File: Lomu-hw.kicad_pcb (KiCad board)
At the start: 2 copper layers, 30 x 26.8 mm, 1 part

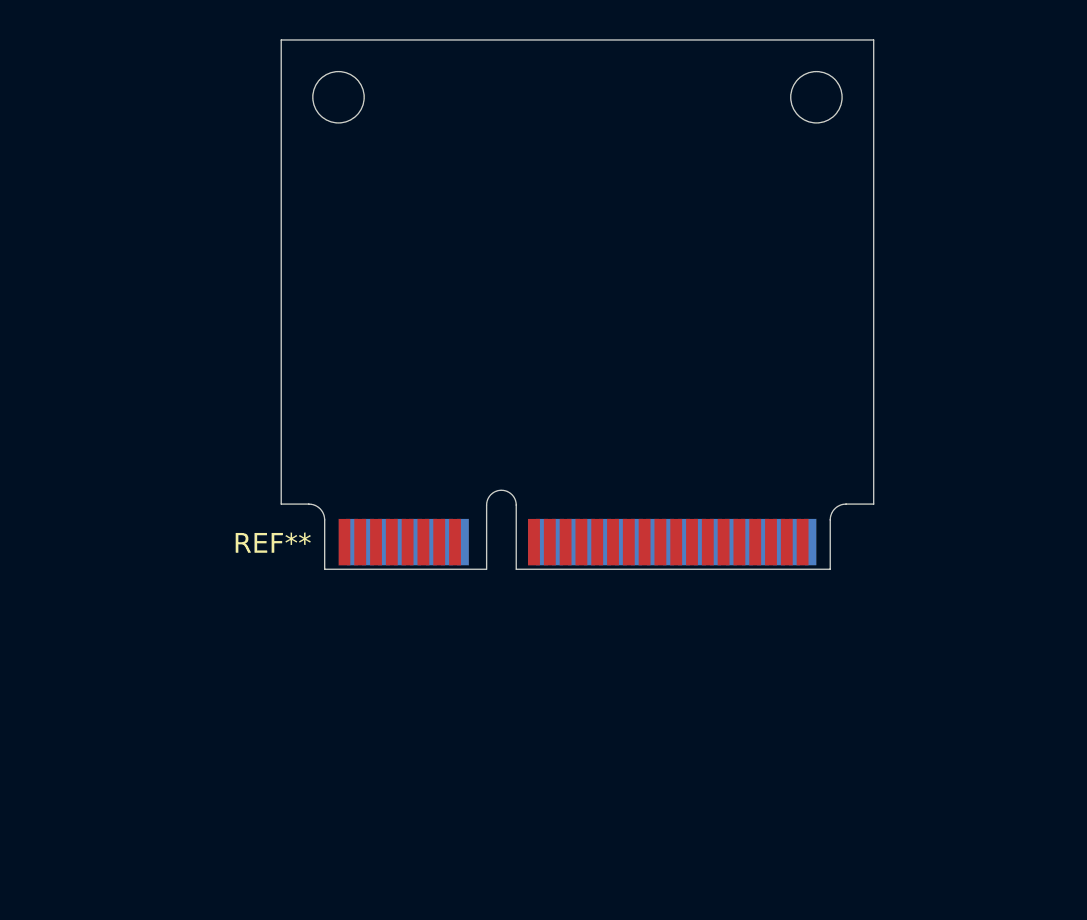
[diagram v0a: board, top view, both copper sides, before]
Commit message: Updates project from mPCIe F1 template
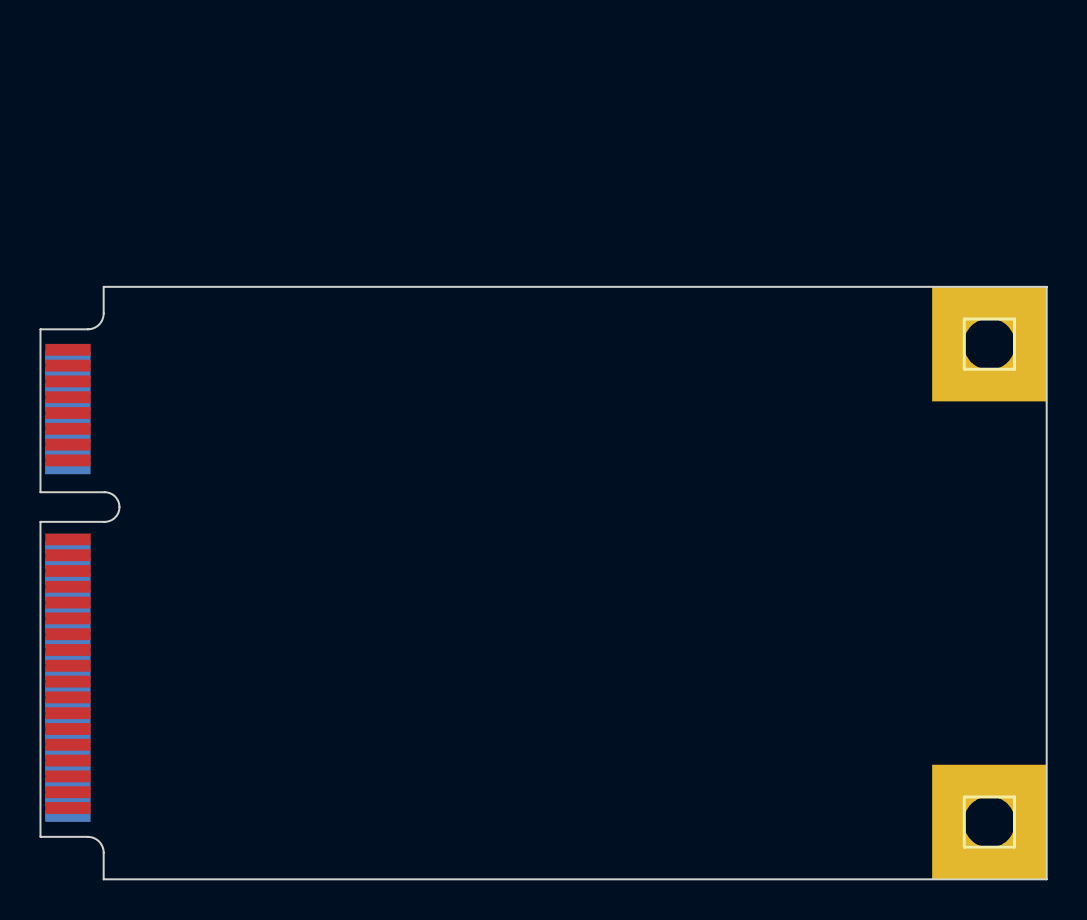
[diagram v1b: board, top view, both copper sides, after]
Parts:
- removed REF**: mini-PCIe_H1_Half, mpcie:mini-PCIe_H1_Half
- added J1: PCIE-MINI, mini-PCIe:miniPCIeConn, F.Cu at (116.5, 61.6)
- added MOUNTING_HOLE1: CONN_1, PIN_ARRAY_1, F.Cu at (163.1, 53.4)
- added MOUNTING_HOLE2: CONN_1, PIN_ARRAY_1, F.Cu at (163.1, 77.6)
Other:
- board size 30 x 26.8 mm -> 50.9 x 30 mm

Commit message: Adds first draft of layout
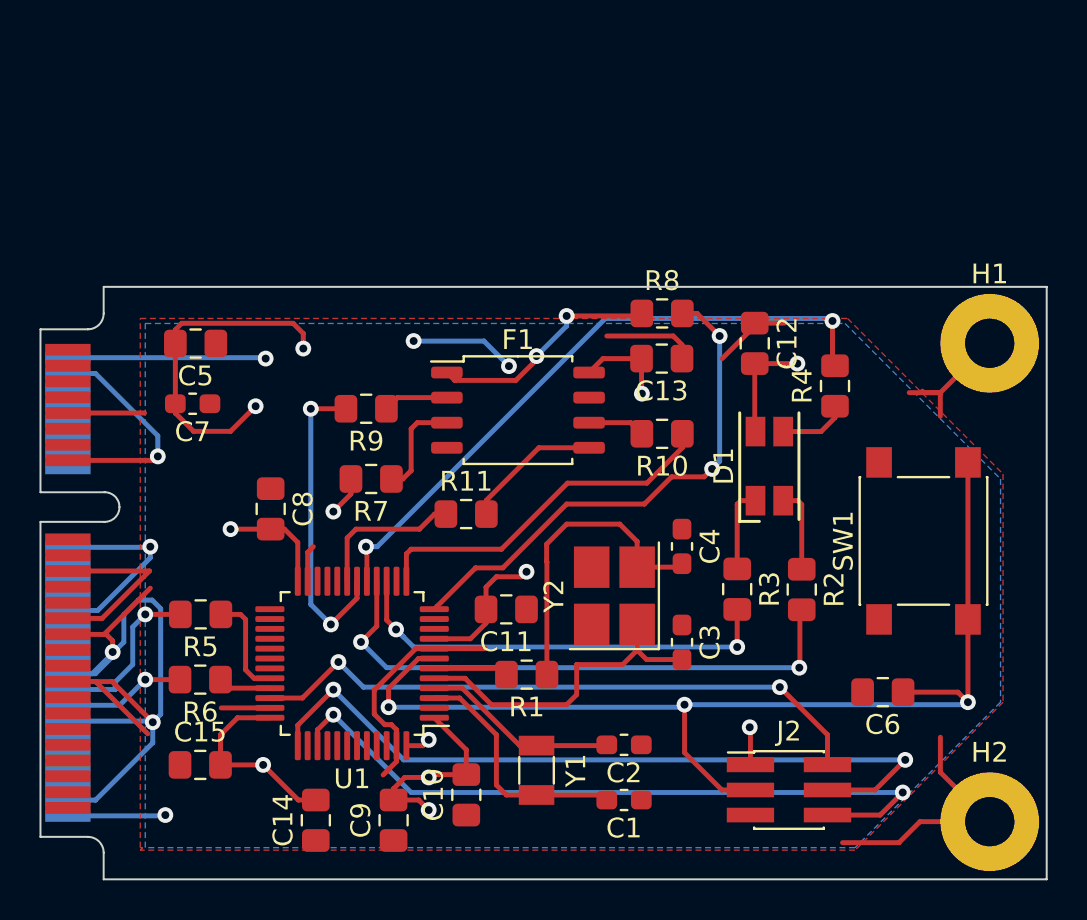
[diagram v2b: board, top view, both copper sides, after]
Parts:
- removed MOUNTING_HOLE1, MOUNTING_HOLE2: CONN_1, PIN_ARRAY_1
- added C1: 10pF, Capacitor_SMD:C_0603_1608Metric_Pad1.05x0.95mm_HandSolder, F.Cu at (144.6, 76.5)
- added C10: 100nF, Capacitor_SMD:C_0805_2012Metric_Pad1.15x1.40mm_HandSolder, F.Cu at (136.7, 76.2)
- added C11: 100nF, Capacitor_SMD:C_0805_2012Metric_Pad1.15x1.40mm_HandSolder, F.Cu at (138.7, 66.8)
- added C12: 100nF, Capacitor_SMD:C_0805_2012Metric_Pad1.15x1.40mm_HandSolder, F.Cu at (151.3, 53.3)
- added C13: 100nF, Capacitor_SMD:C_0805_2012Metric_Pad1.15x1.40mm_HandSolder, F.Cu at (146.5, 54.1)
- added C14: 4.7uF, Capacitor_SMD:C_0805_2012Metric_Pad1.15x1.40mm_HandSolder, F.Cu at (129.0, 77.5)
- added C15: 100nF, Capacitor_SMD:C_0805_2012Metric_Pad1.15x1.40mm_HandSolder, F.Cu at (123.2, 74.7)
- added C2: 10pF, Capacitor_SMD:C_0603_1608Metric_Pad1.05x0.95mm_HandSolder, F.Cu at (144.6, 73.7)
- added C3: 20pF, Capacitor_SMD:C_0603_1608Metric_Pad1.05x0.95mm_HandSolder, F.Cu at (147.6, 68.5)
- added C4: 20pF, Capacitor_SMD:C_0603_1608Metric_Pad1.05x0.95mm_HandSolder, F.Cu at (147.6, 63.6)
- added C5: 100nF, Capacitor_SMD:C_0805_2012Metric_Pad1.15x1.40mm_HandSolder, F.Cu at (122.9, 53.3)
- added C6: 100nF, Capacitor_SMD:C_0805_2012Metric_Pad1.15x1.40mm_HandSolder, F.Cu at (157.7, 71.0)
- added C7: 47pF, Capacitor_SMD:C_0603_1608Metric_Pad1.05x0.95mm_HandSolder, F.Cu at (122.8, 56.4)
- added C8: 100nF, Capacitor_SMD:C_0805_2012Metric_Pad1.15x1.40mm_HandSolder, F.Cu at (126.7, 61.7)
- added C9: 100nF, Capacitor_SMD:C_0805_2012Metric_Pad1.15x1.40mm_HandSolder, F.Cu at (133.0, 77.5)
- added D1: LED_RGBA, LED_SMD:LED_RGB_1210, F.Cu at (152.0, 59.5)
- added F1: MX25V1606FM2I03, Package_SO:SOP-8_5.28x5.23mm_P1.27mm, F.Cu at (139.3, 56.7)
- added H1: MountingHole_Pad, MountingHole:MountingHole_2.5mm_Pad, F.Cu at (163.2, 53.3)
- added H2: MountingHole_Pad, MountingHole:MountingHole_2.5mm_Pad, F.Cu at (163.2, 77.6)
- added J2: ARM_SWD_6, Connector_PinHeader_1.27mm:PinHeader_2x03_P1.27mm_Vertical_SMD, F.Cu at (153.0, 75.9)
- added R1: 390, Resistor_SMD:R_0805_2012Metric_Pad1.15x1.40mm_HandSolder, F.Cu at (139.7, 70.1)
- added R10: 33, Resistor_SMD:R_0805_2012Metric_Pad1.15x1.40mm_HandSolder, F.Cu at (146.6, 57.9)
- added R11: 33, Resistor_SMD:R_0805_2012Metric_Pad1.15x1.40mm_HandSolder, F.Cu at (136.6, 62.0)
- added R2: 1, Resistor_SMD:R_0805_2012Metric_Pad1.15x1.40mm_HandSolder, F.Cu at (153.6, 65.8)
- added R3: 68, Resistor_SMD:R_0805_2012Metric_Pad1.15x1.40mm_HandSolder, F.Cu at (150.4, 65.8)
- added R4: 1, Resistor_SMD:R_0805_2012Metric_Pad1.15x1.40mm_HandSolder, F.Cu at (155.3, 55.5)
- added R5: 22, Resistor_SMD:R_0805_2012Metric_Pad1.15x1.40mm_HandSolder, F.Cu at (123.2, 67.1)
- added R6: 22, Resistor_SMD:R_0805_2012Metric_Pad1.15x1.40mm_HandSolder, F.Cu at (123.2, 70.4)
- added R7: 10k, Resistor_SMD:R_0805_2012Metric_Pad1.15x1.40mm_HandSolder, F.Cu at (131.8, 60.2)
- added R8: 33, Resistor_SMD:R_0805_2012Metric_Pad1.15x1.40mm_HandSolder, F.Cu at (146.6, 51.8)
- added R9: 33, Resistor_SMD:R_0805_2012Metric_Pad1.15x1.40mm_HandSolder, F.Cu at (131.6, 56.6)
- added SW1: SW_Push_Dual, Button_Switch_SMD:SW_Push_1P1T_NO_6x6mm_H9.5mm, F.Cu at (159.8, 63.3)
- added U1: STM32L562CET6, Package_QFP:LQFP-48_7x7mm_P0.5mm, F.Cu at (130.9, 69.5)
- added Y1: 32 kHz, Crystal:Crystal_SMD_3215-2Pin_3.2x1.5mm, F.Cu at (140.2, 75.0)
- added Y2: 16 MHz, Crystal:Crystal_SMD_3225-4Pin_3.2x2.5mm_HandSoldering, F.Cu at (144.2, 66.1)
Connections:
- J1 pad 15: Net-(J1-Pad15) -> GND
- J1 pad 18: Net-(J1-Pad18) -> GND
- J1 pad 2: Net-(J1-Pad2) -> VCC
- J1 pad 21: Net-(J1-Pad21) -> GND
- J1 pad 26: Net-(J1-Pad26) -> GND
- J1 pad 27: Net-(J1-Pad27) -> GND
- J1 pad 29: Net-(J1-Pad29) -> GND
- J1 pad 34: Net-(J1-Pad34) -> GND
- J1 pad 35: Net-(J1-Pad35) -> GND
- J1 pad 4: Net-(J1-Pad4) -> GND
- J1 pad 40: Net-(J1-Pad40) -> GND
- J1 pad 50: Net-(J1-Pad50) -> GND
- J1 pad 52: Net-(J1-Pad52) -> VCC
- J1 pad 9: Net-(J1-Pad9) -> GND
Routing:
- net GND: track 0.00 -> 123.1 mm, vias 0 -> 4
- net VCC: track 0.00 -> 80.1 mm, vias 0 -> 14
- net /NRST: track 0.00 -> 55.5 mm, vias 0 -> 3
- net /TCK_SWCLK: track 0.00 -> 38.6 mm, vias 0 -> 2
- net /TDO_SWO: track 0.00 -> 36.7 mm, vias 0 -> 2
- net /LED3: track 0.00 -> 32.6 mm, vias 0 -> 2
- net /TMS_SWDIO: track 0.00 -> 32.0 mm, vias 0 -> 2
- net /LED2: track 0.00 -> 29.3 mm, vias 0 -> 2
- net /OCTOSPI1_NCS: track 0.00 -> 26.3 mm, vias 0 -> 2
- net /LED1: track 0.00 -> 22.9 mm, vias 0 -> 2
- net /OCTOSPI1_CLK: track 0.00 -> 18.3 mm
- net /OSC_IN: track 0.00 -> 16.6 mm
- net /OCTOSPI1_IO1: track 0.00 -> 15.9 mm, vias 0 -> 2
- net Net-(C4-Pad2): track 0.00 -> 15.6 mm
- net /OSC32_IN: track 0.00 -> 12.4 mm
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- added copper zone on F.Cu, net GND
- added copper zone on B.Cu, net VCC
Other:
- rule trace_min: 0.2 -> 0.25
- rule via_min_size: 0.4 -> 0.5

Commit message: Adds missing boot select trace
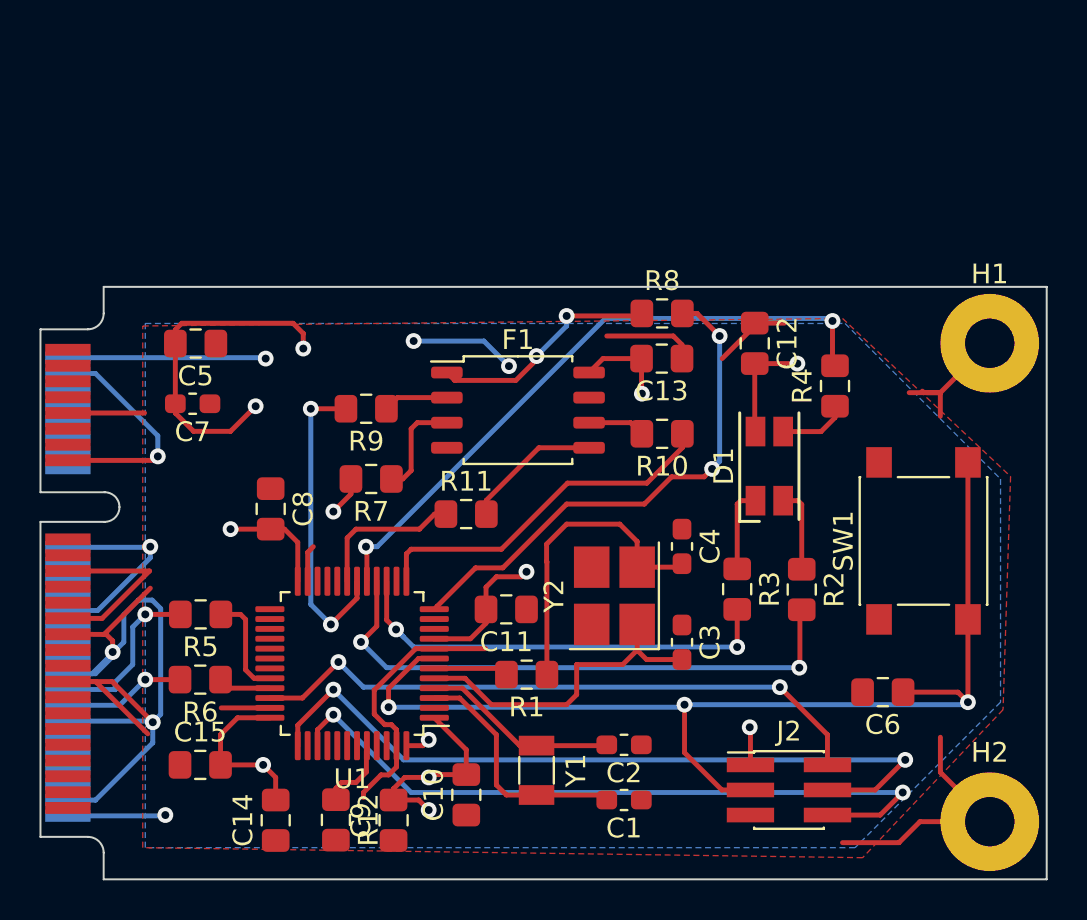
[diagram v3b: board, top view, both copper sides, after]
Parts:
- added R12: 10k, Resistor_SMD:R_0805_2012Metric_Pad1.15x1.40mm_HandSolder, F.Cu at (130.0, 77.5)
- moved C14 2.03 mm to (127.0, 77.5)
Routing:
- net Net-(R12-Pad1): track 0.00 -> 3.81 mm
- net GND: track 123.1 -> 124.9 mm
- net VCC: track 80.1 -> 78.8 mm
